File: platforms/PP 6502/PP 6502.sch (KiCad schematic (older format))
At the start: 21 parts, among them J1 Signals, J3 SBC, J4 ADDRESS, J5 Port A, J6 Port B, J7 PWR1, J8 PWR2, M1 Mounting, M2 Mounting, M3 Mounting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

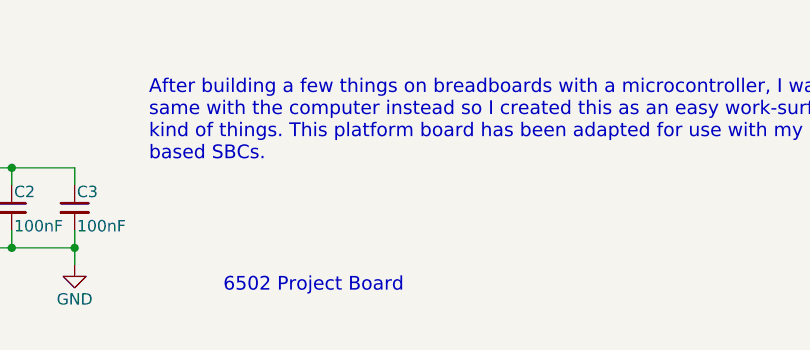
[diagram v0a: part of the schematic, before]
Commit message: Reorganized libraries
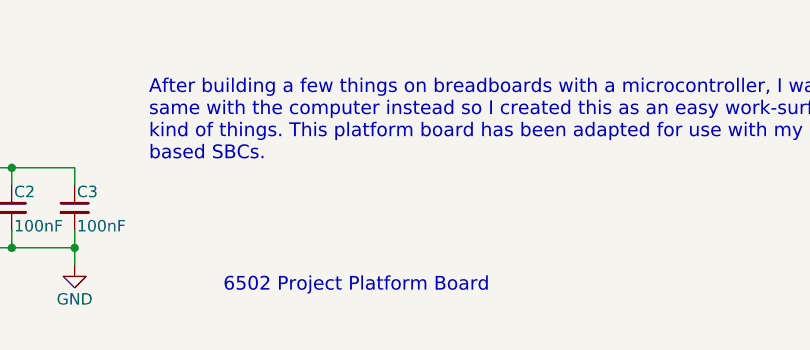
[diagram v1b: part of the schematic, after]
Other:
- note added: "6502 Project Platform Board"
- note removed: "6502 Project Board"
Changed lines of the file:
@@
 LIBS:mounting
 LIBS:rc1_backplane
+LIBS:6522
 LIBS:breadboard
-LIBS:6522
-LIBS:6502 Project Board-cache
+LIBS:PP 6502-cache
 EELAYER 25 0
 EELAYER END
@@
 $EndComp
 Text Notes 12175 10925 0    60   ~ 0
-6502 Project Board
+6502 Project Platform Board
 Entry Wire Line
 	14325 5300 14225 5400

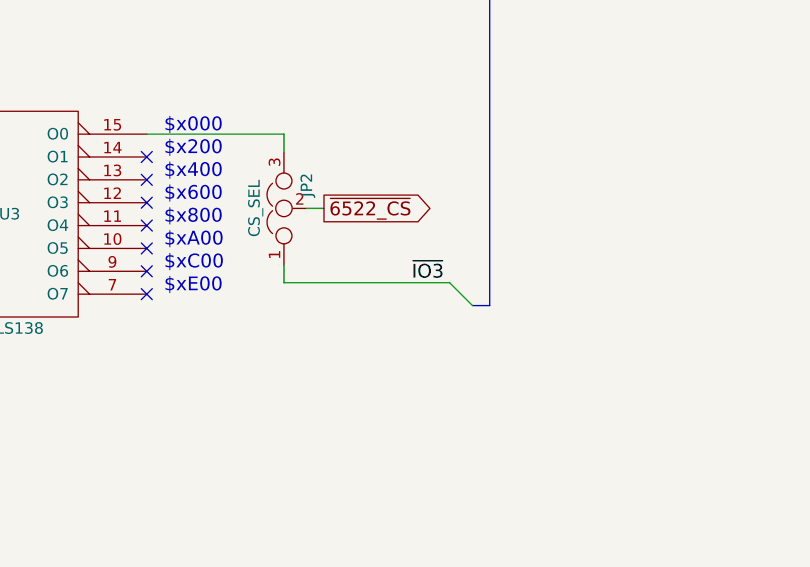
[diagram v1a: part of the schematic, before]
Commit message: Silkscreen tweaks
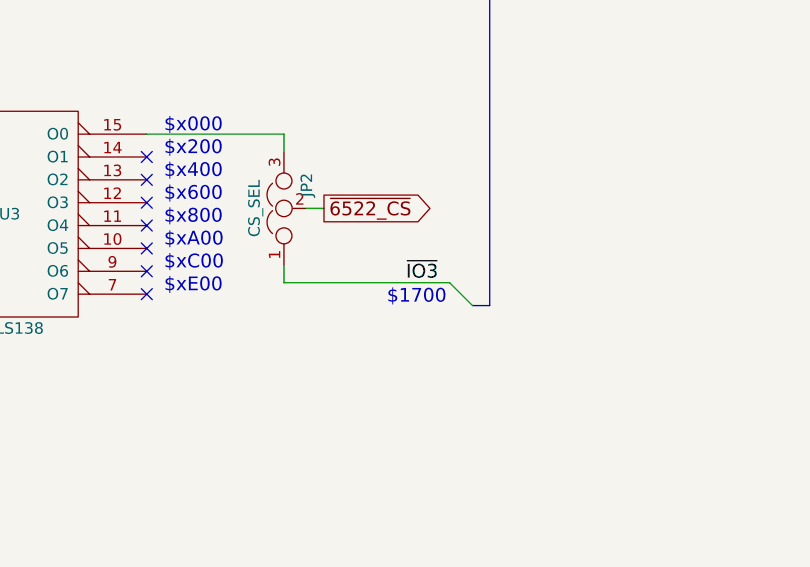
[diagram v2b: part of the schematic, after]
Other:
- note added: "$1700"
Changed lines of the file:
@@
 	0    -1   -1   0
 $EndComp
-Text Label 7200 2550 2    60   ~ 0
+Text Label 7175 2550 2    60   ~ 0
 ~IO3
 Wire Wire Line
@@
 Text Notes 850  4100 0    60   ~ 0
 6522 clock selection jumper, solder\na link from 1-2 for most 6502-based\ncomputers. 2-3 for 6800-based CPUs.
+Text Notes 6950 2650 0    60   ~ 0
+$1700
 $EndSCHEMATC

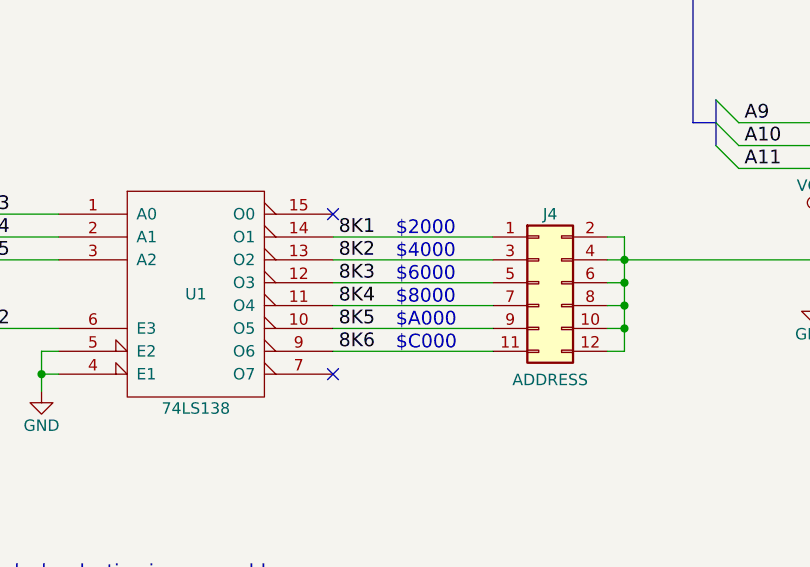
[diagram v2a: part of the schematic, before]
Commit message: Fixed 6502 address calculations
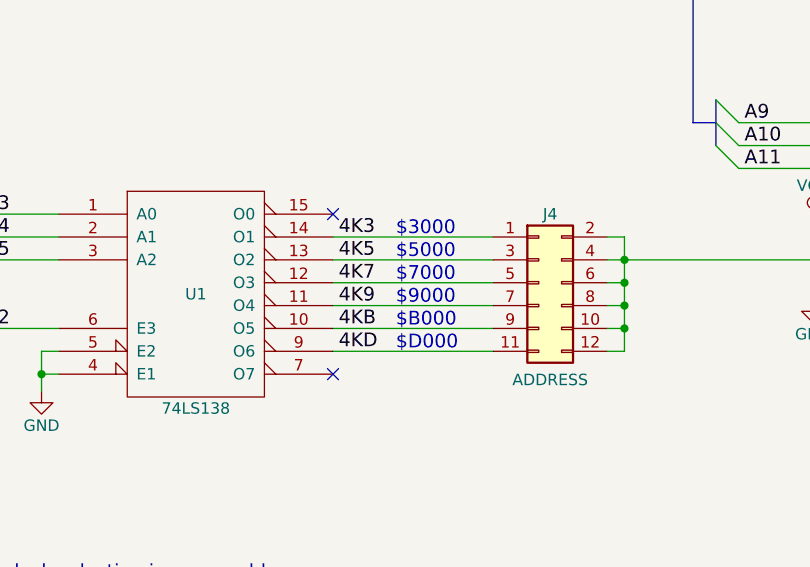
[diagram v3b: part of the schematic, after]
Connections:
- net 8K1 renamed 4K3
- net 8K2 renamed 4K5
- net 8K3 renamed 4K7
- net 8K4 renamed 4K9
- net 8K5 renamed 4KB
- net 8K6 renamed 4KD
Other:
- note added: "$3000"
- note added: "$5000"
- note added: "$7000"
- note added: "$9000"
- note added: "$B000"
- note added: "$D000"
- note removed: "$2000"
- note removed: "$4000"
- note removed: "$6000"
- note removed: "$8000"
- note removed: "$A000"
- note removed: "$C000"
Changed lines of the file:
@@
 $EndComp
 Text Label 2550 2400 0    60   ~ 0
-8K1
+4K3
 Text Label 2550 2500 0    60   ~ 0
-8K2
+4K5
 Text Label 2550 2600 0    60   ~ 0
-8K3
+4K7
 Entry Wire Line
 	825  2200 925  2300
@@
 	825  2400 925  2500
 Text Notes 2800 2400 0    60   ~ 0
-$2000
+$3000
 Text Notes 2800 2500 0    60   ~ 0
-$4000
+$5000
 Text Notes 2800 2600 0    60   ~ 0
-$6000
+$7000
 Text Notes 2800 2700 0    60   ~ 0
-$8000
+$9000
 Text Notes 2800 2800 0    60   ~ 0
-$A000
+$B000
 Text Notes 2800 2900 0    60   ~ 0
-$C000
+$D000
 Text Label 2550 2700 0    60   ~ 0
-8K4
+4K9
 Text Label 2550 2800 0    60   ~ 0
-8K5
+4KB
 Text Label 2550 2900 0    60   ~ 0
-8K6
+4KD
 NoConn ~ 2525 2300
 $Comp
